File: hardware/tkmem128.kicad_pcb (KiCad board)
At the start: 2 copper layers, 78.7 x 66 mm, 24 parts, among them J1 Barramento TK, U1 GAL20V8B, U2 74HCT273, U3 AS6C1008-55PCN, U4 27C256

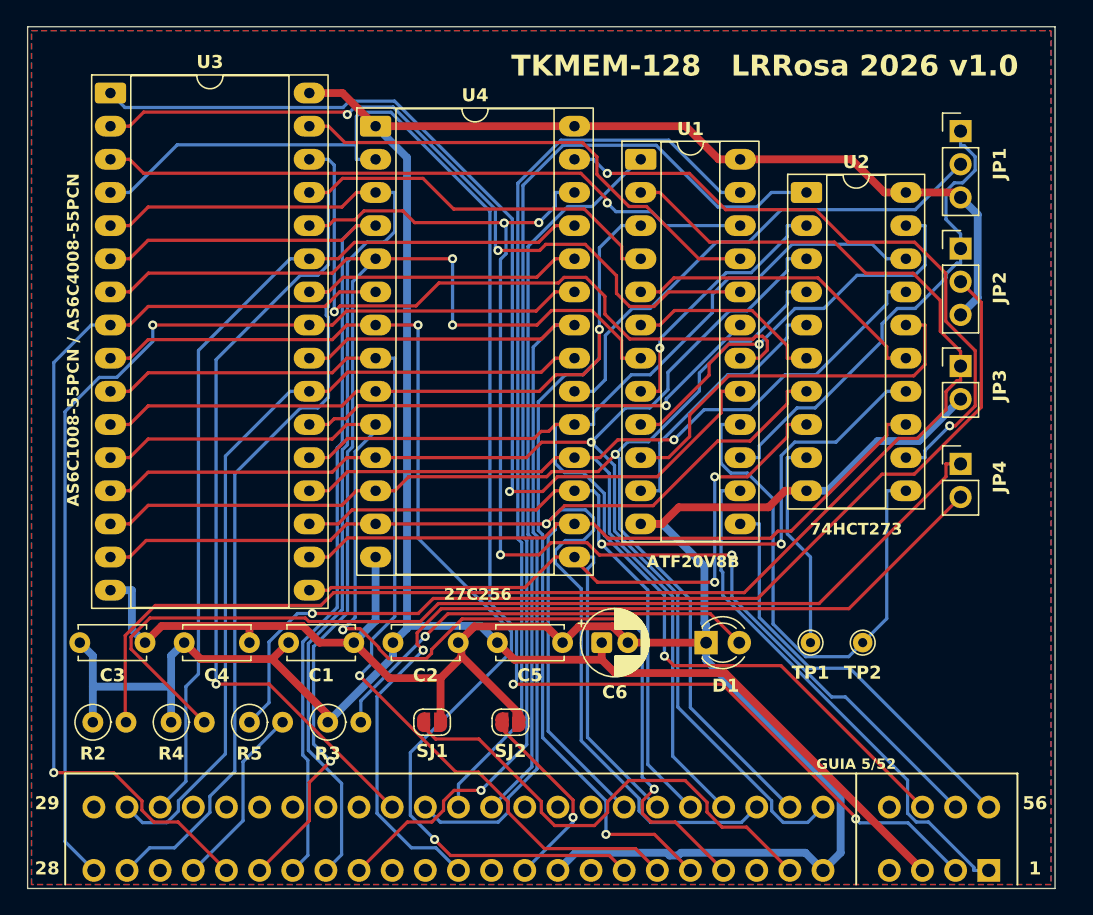
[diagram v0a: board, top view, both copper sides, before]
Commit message: Principal: trilha 0,50 mm, reposicionada para rotear
Voce estava certo nos dois pontos. Medindo o que estava la: dos 96 vaos entre
ilhas vizinhas de DIP, 10 tinham 2 ou 3 trilhas passando. E a ilha LongPads
deixa 0,94 mm de vao, onde cabe EXATAMENTE UMA trilha em qualquer largura
sensata — 0,25/0,15 precisava de 0,95 mm para duas. O autorouter espremeu onde
nao cabia.

REGRAS      sinal 0,25 -> 0,50 mm | alimentacao 0,60 -> 1,00 | isolacao 0,14 ->
            0,20. Com isso o canal duplo entre ilhas fica proibido por
            construcao, e nao por sorte.

POSICIONAMENTO. O arranjo velho tinha DUAS fileiras de passivos atravessando a
placa de lado a lado (C1..C6+D1+TP em y=47,2; R2..SJ2 em y=53,3), bem entre o
conector e os CIs — por onde passam A0..A13 e D0..D7. E os cinco capacitores de
desacoplamento ficavam a 40 mm dos pinos que deveriam desacoplar.

Os quatro CIs tambem estavam VERTICAIS: os 16 pinos de um lado empilhados numa
reta de 38 mm, obrigando todo sinal vindo do conector a subir por um canal
estreito ao lado do CI e depois virar. Girados para HORIZONTAL, a fileira de
pinos fica paralela ao conector e cada sinal sobe quase reto — e o que a placa
Luccas faz, e e por isso que as trilhas dela podem ser gordas.

  y  4..22   U4 EPROM (horizontal)     |  JP1..JP4, R2..R5, D1, TP1, TP2
  y 27..45   U3 SRAM  (horizontal)     |  U1 GAL / U2 74HCT273
  y 48..57   corredor limpo de ponta a ponta
  y 60..65   conector

Cada capacitor de desacoplamento foi para junto do pino de +5V do seu CI.

SJ1 E SJ2 SAIRAM (sua sugestao, e estava certa). Eram terra extra OPCIONAL em
pinos que so sao GND numa das maquinas — 7 no ZX Spectrum, 15 no TK — e a
propria documentacao ja mandava deixar os dois abertos. Em troca, cada um puxava
uma rede do conector ate o outro extremo da placa. Sozinha essa remocao nao
fechou as ultimas nets, mas simplificou a placa e eliminou uma colisao de
contorno com C5. Quem quiser o terra extra solda um fio do pino ao plano.

BUG NO PIPELINE, ach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
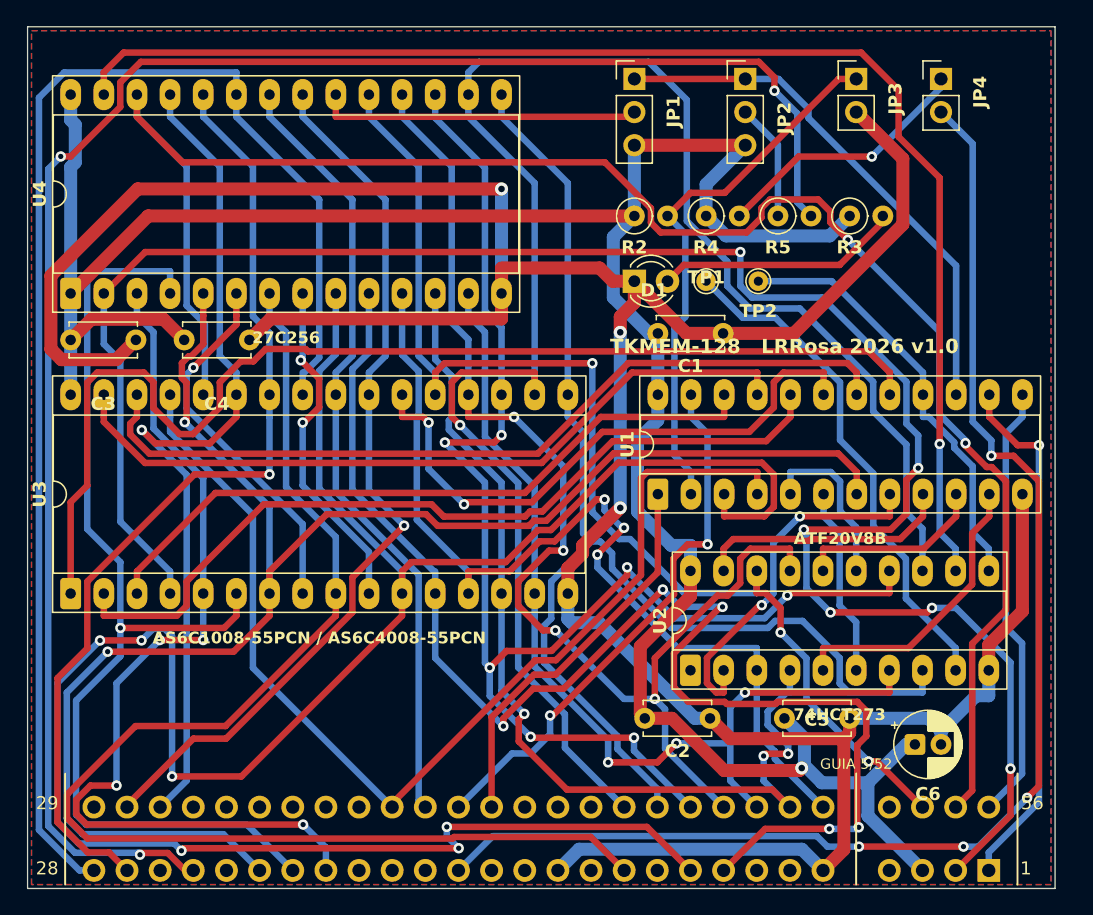
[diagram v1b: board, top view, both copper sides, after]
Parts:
- removed SJ1: GND pino 7, SolderJumper-2_P1.3mm_Open_RoundedPad1.0x1.5mm
- removed SJ2: GND pino 15, SolderJumper-2_P1.3mm_Open_RoundedPad1.0x1.5mm
- moved R2 56.8 mm to (46.5, 14.5)
- moved R4 56.4 mm to (52.0, 14.5)
- moved R5 56.1 mm to (57.5, 14.5)
- moved R3 55.7 mm to (63.0, 14.5)
- moved U3 38.5 mm to (3.30, 43.4), turned to 90 degrees
- moved U2 37.7 mm to (50.8, 49.3), turned to 90 degrees
- moved C1 36.9 mm to (48.3, 23.5)
- moved JP4 29.5 mm to (70.0, 4.00)
- moved TP1 28.8 mm to (52.0, 19.5)
- moved TP2 28.8 mm to (56.0, 19.5)
- moved D1 28.2 mm to (46.5, 19.5)
- moved U4 26.7 mm to (3.30, 20.4), turned to 90 degrees
- moved U1 25.7 mm to (48.3, 35.8), turned to 90 degrees
- moved JP1 25.3 mm to (46.5, 4.00)
- moved C6 25.2 mm to (68.0, 55.0)
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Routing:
- net ROMCS_BUS: track 14.2 -> 135.4 mm, vias 0 -> 3
- net GND: track 158.6 -> 245.5 mm, vias 0 -> 3
- net RESET_N: track 85.7 -> 0.00 mm, vias 1 -> 0
- net A1: track 103.1 -> 178.8 mm, vias 2 -> 6
- net ZX512: track 112.7 -> 41.6 mm
- net ROMCS_DRV: track 79.1 -> 9.00 mm, vias 1 -> 0
- net D4: track 77.3 -> 137.3 mm, vias 0 -> 1
- net RAMDIS_DRV: track 78.7 -> 20.2 mm, vias 0 -> 1
- net ROMA14: track 50.4 -> 103.1 mm, vias 2 -> 1
- net A2: track 77.8 -> 26.2 mm, vias 1 -> 2
- net A4: track 75.1 -> 28.3 mm
- net A13: track 94.0 -> 139.3 mm, vias 4 -> 2
- net A12: track 115.6 -> 153.3 mm, vias 2 -> 6
- net BUS_P07: track 37.3 -> 0.00 mm
- net RAMDIS: track 69.5 -> 103.6 mm, vias 1 -> 4
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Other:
- board text removed: "SJ1 e SJ2 são terra extra, opcionais - podem ficar abertos"
- board text removed: "SJ1 fechar SÓ em ZX Spectrum (pino 7 = GND lá)"
- board text removed: "SJ2 fechar SÓ em TK90X/TK95 (pino 15 = GND lá)"

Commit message: Ilhas dedicadas para os tres fios de ligacao
Voce tem razao: fio soldado em cima da perna de outro componente parece conserto
de erro, nao projeto. Cada uma das tres ligacoes ganhou um PAR DE ILHAS PROPRIAS,
com o nome da rede na serigrafia ao lado.

  A4       par de ilhas marcado A4      face do cobre         ~23 mm
  A2       par de ilhas marcado A2      face dos componentes  ~26 mm
  RESET    par de ilhas marcado RESET   face do cobre         ~28 mm

As duas ilhas de um par caem sempre na MESMA face — senao o fio teria de
contornar a placa. Cada ilha se liga ao cobre da sua rede por um coto reto de
0,5 mm com 1,6 mm de comprimento.

ILHA SMD, NAO PASSANTE, de proposito. Tentei passante primeiro: junto do
conector nao existe um milimetro livre nas duas faces ao mesmo tempo — sao 54
ilhas passantes a 2,54 mm de passo, e as tres pontas do lado do conector nao
acharam lugar em 9 mm de raio. Numa face so, todas as seis couberam a 1,6 mm da
sua ancora.

Como as posicoes foram achadas: `busca_ilhas.py` monta o mapa de cobre ocupado
das duas faces e, para cada ponta, varre em circulos crescentes ate achar um
ponto onde (a) a ilha cabe com 0,20 mm de folga de tudo que nao e da rede, e
(b) o coto reto ate a ancora tambem passa. Depois testa as duas faces e fica com
a que serve para as DUAS pontas do par.

Serigrafia: primeiro desenhei um tracejado ligando cada par. Ficou ruim — uma
linha de 25 mm atravessa metade da serigrafia da placa e gerou 13 sobreposicoes.
Trocado pelo nome da rede ao lado de cada ilha, e a referencia W1..W6 escondida
(nao ajuda quem solda, e so colidia com o rotulo).

DRC: 4 violacoes, contra 8 antes. Sao 3 de alivio termico, 1 de serigrafia e as
3 "desconexoes" que SAO os vaos dos fios — o KiCad nao tem como representar um
fio voador. Zero isolacao, zero curto, zero cobre-na-borda.

Corrigido de quebra: PCB_VIA::GetWidth() sem argumento de camada dispara assert
no KiCad 10 e derruba o processo. Era o que estava abrindo aquelas caixas de
"wxWidgets 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
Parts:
- added W1: WirePad_1.6mm, WirePad_1.6mm, B.Cu at (14.2, 63.5)
- added W2: WirePad_1.6mm, WirePad_1.6mm, B.Cu at (21.5, 41.9)
- added W3: WirePad_1.6mm, WirePad_1.6mm, F.Cu at (47.2, 63.5)
- added W4: WirePad_1.6mm, WirePad_1.6mm, F.Cu at (26.5, 45.0)
- added W5: WirePad_1.6mm, WirePad_1.6mm, B.Cu at (25.5, 63.1)
- added W6: WirePad_1.6mm, WirePad_1.6mm, B.Cu at (51.2, 50.9)
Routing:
- net A4: track 28.3 -> 31.5 mm
- net A2: track 26.2 -> 29.4 mm
- net RESET_N: track 0.00 -> 3.19 mm
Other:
- board text added: "A2"
- board text added: "A4"
- board text added: "RESET"

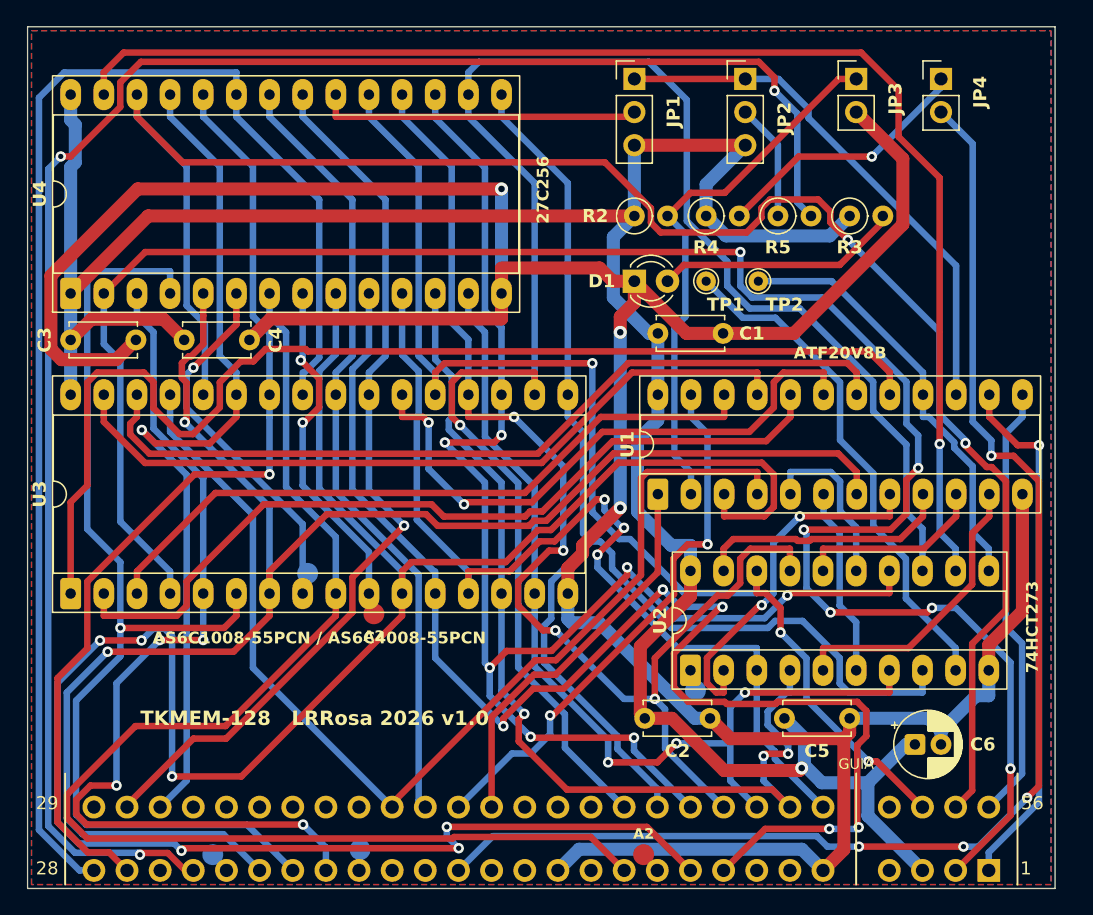
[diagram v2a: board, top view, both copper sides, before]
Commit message: Placa principal em 4 camadas: 100% roteada, zero fio
  F.Cu    sinal
  In1.Cu  plano de GND inteiro
  In2.Cu  plano de +5V inteiro
  B.Cu    sinal

Como todos os componentes sao passantes, cada ilha de +5V e de GND toca o seu
plano direto: nao ha uma unica trilha de alimentacao nas faces de sinal, nem via
que sirva so para alimentacao. As duas faces ficam inteiras para sinal.

MAS as 4 camadas sozinhas nao resolveram nada — continuou em 3 nets em aberto,
as mesmas de sempre. Foi isso que finalmente expos a causa raiz, que eu vinha
atacando pelo lado errado o tempo todo:

  As ilhas do conector tinham 1,75 mm num passo de 2,54, deixando 0,79 mm entre
  vizinhas. Uma trilha de 0,50 com 0,20 de isolacao precisa de 0,90 mm. Para
  sair da fileira de BAIXO do conector, um sinal tem que passar entre duas
  ilhas da fileira de cima — e nao cabia. NENHUM sinal conseguia escapar por
  ali. Por isso as mesmas tres nets falhavam com qualquer largura (testei ate
  0,40 mm), qualquer isolacao e quatro arranjos de componentes diferentes.

Ilha de J1 para 1,50 mm: o vao vai a 1,04 mm e a trilha passa com 0,27 de folga
de cada lado. Anel remanescente (1,50-1,02)/2 = 0,24 mm, folgado para qualquer
fabricante. So isso levou de 3 para 1 net em aberto; a ultima fechou perturbando
a isolacao do DSN para 0,215.

RESULTADO   74 de 74 nets roteadas, trilha de 0,50 mm, 39 vias.
            DRC 0 violacoes, 0 desconexoes. ERC 0.
            Nenhum fio de ligacao. Saiu tambem o par de ilhas W1..W6 do commit
            anterior, que nao serve mais para nada.

Os avisos de alivio termico sumiram junto: nao ha mais ilha de alimentacao
ligada a plano por raios, elas mergulham direto no plano interno.

GERBERS EM .ZIP, que voce notou que faltavam: `tools/producao.sh` regenera tudo
das duas placas e fecha `production/*/gerbers.zip`. Rodar sempre que a placa
mudar, ate por ajuste de serigrafia. O zip e feito por Python porque o Git Bash
do Windows nao traz o utilitario `zip`.

As camadas internas f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
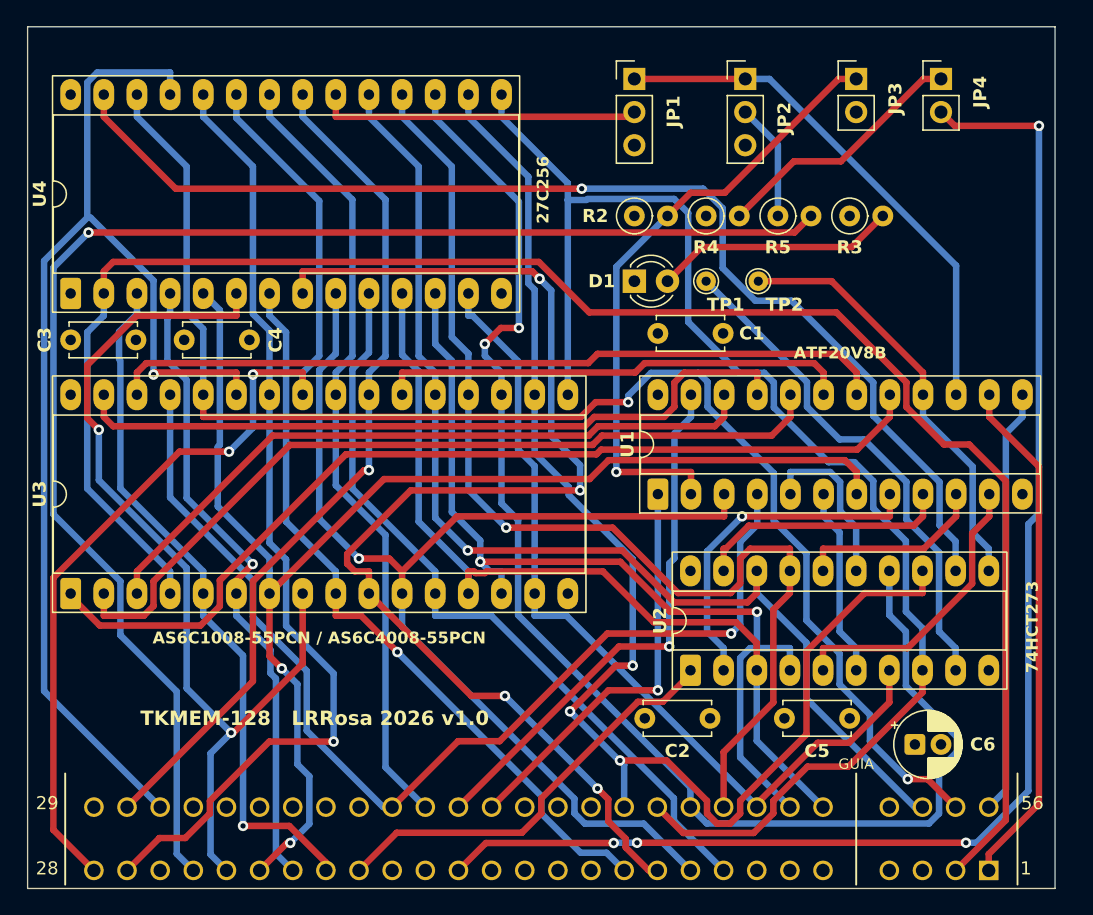
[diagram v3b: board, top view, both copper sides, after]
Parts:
- removed W1, W2, W3, W4, W5, W6: WirePad_1.6mm, WirePad_1.6mm
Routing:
- net GND: track 245.5 -> 0.00 mm, vias 3 -> 0
- net +5V: track 194.7 -> 0.00 mm, vias 1 -> 0
- net A1: track 178.8 -> 88.7 mm, vias 6 -> 1
- net A2: track 29.4 -> 94.1 mm, vias 2 -> 4
- net A0: track 104.9 -> 59.0 mm, vias 5 -> 0
- net A3: track 99.3 -> 57.8 mm, vias 0 -> 1
- net A4: track 31.5 -> 72.2 mm, vias 1 -> 2
- net D4: track 137.3 -> 103.3 mm, vias 1 -> 3
- net A6: track 81.1 -> 49.3 mm
- net A13: track 139.3 -> 108.8 mm
- net RESET_N: track 3.19 -> 32.6 mm
- net A11: track 105.3 -> 79.6 mm, vias 0 -> 2
- net A5: track 125.9 -> 100.7 mm
- net ROMCS_BUS: track 135.4 -> 110.3 mm, vias 3 -> 1
- net A8: track 66.5 -> 91.4 mm
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- added copper zone on In2.Cu, net +5V
- added copper zone on In1.Cu, net GND
- removed copper zone on B.Cu, net GND
- removed copper zone on F.Cu, net GND
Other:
- copper layers 2 -> 4
- board text removed: "A2"
- board text removed: "A4"
- board text removed: "RESET"

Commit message: Auto-desativacao vai para o pino 29; JP4 deixa de existir
Sua pesquisa resolve o pior risco que sobrava no projeto. Conferi antes de mexer,
porque errar isso custa o micro de quem monta:

  Pinagem oficial do TK, arquivada em docs/ (imagem, extraida do PDF do Luccas):
  o pino 29 esta marcado **N.C.**  E nas fotos do cartao do TK o dedo 29, como o
  17, nao tem trilha nenhuma chegando.

  O lado do Spectrum (28A livre) e a sua pesquisa. Vale registrar que o busdef
  deste projeto sinaliza TODO pino que difere entre as duas maquinas — 16/17/18
  como Y/V/U do video, 34/35/37 como alimentacao divergente — e o 29 nunca teve
  ressalva nenhuma. Duas fontes independentes concordando.

Com o pino 29 sendo N.C. nas DUAS maquinas, o pull-up pode ser PERMANENTE: num
Spectrum nao ha nada ligado ali, num TK ele faz o que tem que fazer. Entao:

  JP4 SAIU. Com ele saiu o aviso "NUNCA feche JP4 em ZX Spectrum" da serigrafia,
  do README, do MONTAGEM e do PREPARAR-O-TK. Nao existe mais posicao errada para
  escolher — o risco nao foi mitigado, foi eliminado.

R4 fica, e continua em 1k: e o limite de corrente, e nao monta-lo libera o pino
29 para quem precisar dele. Conferi que 1k basta: a placa Luccas original usava
10k nesse mesmo ponto e funcionava, o que prova que o pino 10 do IC27 e entrada
livre, sem nada disputando.

UM DETALHE PRATICO que a documentacao agora avisa: o pino 29 esta na fileira de
CIMA (29..56), na face do cartao do TK oposta a dos pinos 1..28. Quem seguir as
fotos da modificacao original vai soldar do outro lado da placa-mae.

REROTEAMENTO. A mudanca de pino move a rede para o canto oposto da placa, entao a
principal foi reroteada inteira. O Freerouting fechou 73 das 74 e deixou A14 —
que nao era a rede alterada, e a diferenca de 1 net entrou no ruido do
determinismo dele. Fiz A14 a mao pela margem direita, com um detalhe medido: a
janela entre a ilha do GAL (que acaba em x=77,44) e a folga de borda tem 0,30 mm
de largura, e a trilha de 0,5 mm cabe centrada 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
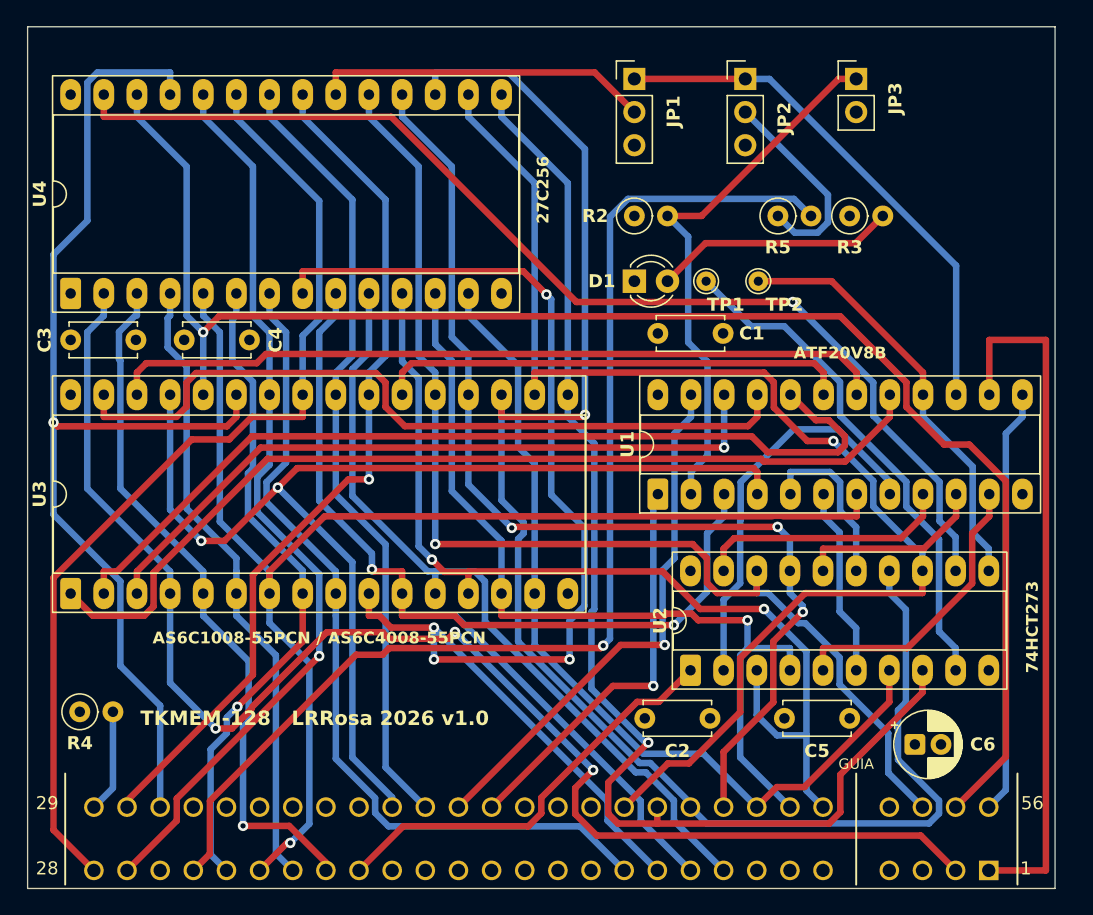
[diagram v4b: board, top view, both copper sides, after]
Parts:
- removed JP4: AUTO-DESATIVA 32K, PinHeader_1x02_P2.54mm_Vertical
- moved R4 61.2 mm to (4.00, 52.5)
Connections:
- J1 pad 17: RAMDIS -> BUS_P17
- J1 pad 29: BUS_P29 -> RAMDIS
- R4 pad 2: RAMDIS_DRV -> RAMDIS
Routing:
- net RAMDIS: track 105.4 -> 7.91 mm, vias 4 -> 0
- net A12: track 136.8 -> 109.6 mm, vias 0 -> 3
- net A4: track 72.2 -> 50.3 mm, vias 2 -> 1
- net ROMCS_BUS: track 110.3 -> 90.5 mm
- net RAMDIS_DRV: track 19.8 -> 0.00 mm
- net D5: track 106.9 -> 123.1 mm, vias 2 -> 1
- net A14: track 39.6 -> 53.6 mm
- net D3: track 107.3 -> 94.6 mm, vias 0 -> 1
- net A13: track 108.8 -> 120.0 mm, vias 2 -> 1
- net D0: track 66.0 -> 75.0 mm, vias 0 -> 2
- net A3: track 57.8 -> 65.3 mm, vias 1 -> 0
- net A8: track 91.4 -> 84.5 mm
- net ROMCS_DRV: track 9.00 -> 15.8 mm
- net SA16: track 63.4 -> 69.7 mm
- net A1: track 88.7 -> 94.6 mm, vias 1 -> 2
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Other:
- board text added: "R4: pull-up do pino 29 (auto-desativa a RAM de 32K do TK)"
- board text removed: "JP4 fechado = auto-desativa a RAM de 32K do TK"
- board text removed: "NUNCA feche JP4 em ZX Spectrum"
